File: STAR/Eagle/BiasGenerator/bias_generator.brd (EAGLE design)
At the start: 54.6 x 29.8 mm, 24 parts, among them J1 J30J-9J30, T1 750311838, U1 LT8300, U2 LT8330

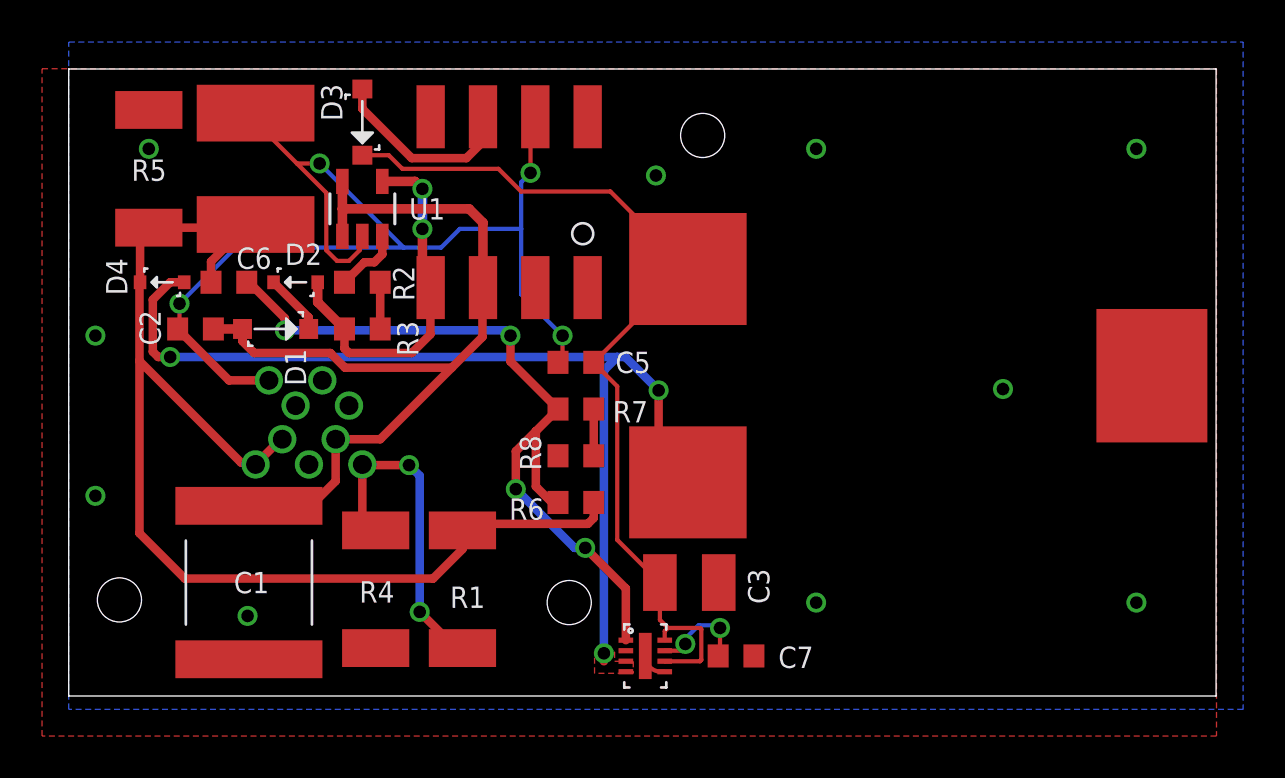
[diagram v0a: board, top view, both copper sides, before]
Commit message: Finished routing new bias board rev 2.0. Fixed the choke configuration on that board.
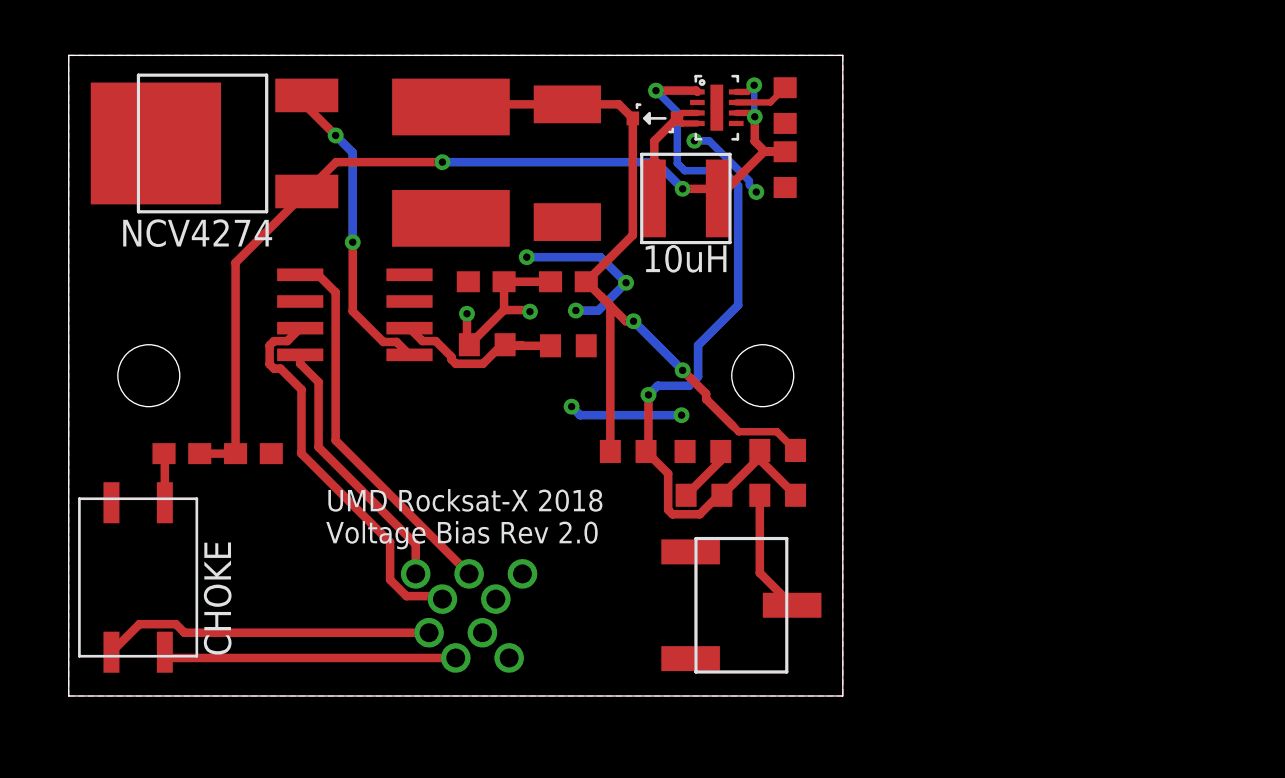
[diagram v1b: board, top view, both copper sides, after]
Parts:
- removed C1: 22uF, AR_passives:3025
- removed C2, C5, C7: 1uF, AR_passives:0603
- removed C3: (no value), resistor:C1210
- removed C4: 10uF, AR_passives:2J-LEAD
- removed C6: 4.7pF, AR_passives:0603
- removed D1: MMSZ5266BT1G, AR_diode:SOD123
- removed D2: BAV20W, AR_diode:SOD323
- removed D3: SBR0560S1, AR_diode:SOD123
- removed D4: PMEG6010CEJ, AR_diode:SOD323
- removed L1: 10uH, AR_passives:PQ2614
- removed R1: 47k, resistor:R2512
- removed R2: 407k, resistor:R0603
- removed R3: 1k, resistor:R0603
- removed R4: 3k, resistor:R2512
- removed R5: 1.5k, resistor:R2512
- removed R6: 1M, resistor:R0603
- removed R7: 33k, resistor:R0603
- removed R8: 52.6, resistor:R0603
- removed T1: 750311838, AR_transformer:750311838
- removed U1: LT8300, AR_IC:SOT23-5
- removed U2: LT8330, AR_IC:8-DFN
- added CHOKE: DFT7160-105B, Filtering:DFT7160
- added C_GND, C_VCC: .1uF, resistor:C0603
- added C_LAD: 4.7pF, AR_passives:0603
- added C_LTIN, C_LTREQ: 1uF, AR_passives:0603
- added C_LTOUT: 10uF, AR_passives:2J-LEAD
- added D_LT: PMEG6010CEJ, AR_diode:SOD323
- added ISO: AMC1311-Q1, Filtering:SOIC8
- added L_LT: ASPI-4020S-100M-T, AR_passives:4MM
- added L_VCC, L_VOUT: 82nH, resistor:C0603
- added REG: NCV4274ADT50RKG, Filtering:DPAK
- added R_DIV1: 500k, resistor:R0603
- added R_DIV2: 25k, resistor:R0603
- added R_LAD1: 1M, resistor:R0603
- added R_LAD2: 33k, resistor:R0603
- added R_LAD3: 52.6, resistor:R0603
- added R_LTOUT: 1.5k, resistor:R2512
- added R_POT1: 20k, resistor:R0603
- added R_POT2: 3269W-1-503LF, Filtering:POTENTIOMETER
- added SWITCH: LT8330, AR_IC:8-DFN
- moved J1 12.0 mm to (19.1, 3.81), turned to 180 degrees
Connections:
- removed net +20V: C3.1, C5.1, D3.P$2, L1.P$2, U2.P$6, U2.P$8
- removed net N$10: J1.9
- removed net N$3: R2.2, R3.1
- removed net N$4: D2.P$1, R3.2, T1.P$4, U1.4
- removed net N$5: D3.P$1, T1.P$6
- removed net N$6: C7.1, U2.P$7
- removed net N$7: D4.P$1, L1.P$3, U2.P$3, U2.P$4
- removed net N$9: C6.2, R6.1, R7.2, U2.P$1
- new net +50V_FILT: C_GND.1, J1.1, J1.2, L_VOUT.2, R_DIV1.2
- new net 5V_REG: ISO.1, REG.P$3
- new net FBX: C_LAD.2, R_LAD1.1, R_LAD2.2, R_POT1.2, SWITCH.P$1
- new net GND_IN: CHOKE.P$1, J1.9
- new net INTVCC: C_LTREQ.1, SWITCH.P$7
- new net STAR_3V3: ISO.8, J1.5
- new net STAR_GND: ISO.5, J1.3
- new net SW: D_LT.P$1, L_LT.P$2, SWITCH.P$3, SWITCH.P$4
- new net VCC_FILT: C_LTIN.1, C_VCC.1, L_LT.P$1, L_VCC.2, REG.P$1, SWITCH.P$6, SWITCH.P$8
- new net V_SENSE: ISO.7, J1.4
- net +50V: now also C_LAD.1, C_LTOUT.P$1, D_LT.P$2, L_VOUT.1, R_LAD1.2, R_LTOUT.2; no longer C4.P$1, C6.1, D4.P$2, J1.1, J1.2, R1.2, R5.2, R6.2
- net GND: now also CHOKE.P$4, C_GND.2, C_LTIN.2, C_LTOUT.P$2, C_LTREQ.2, C_VCC.2, ISO.4, REG.P$4, R_DIV2.1, R_LAD3.1, R_LTOUT.1, R_POT2.P$3, SWITCH.P$5, SWITCH.P$9; no longer C1.P$2, C2.2, C3.2, C4.P$2, C5.2, C7.2, R4.1, R5.1, R8.1, T1.P$7, U1.2, U2.P$5, U2.P$9
- net N$1: now also CHOKE.P$3, L_VCC.1; no longer D1.P$2, D2.P$2
- net N$11: now also R_LAD2.1, R_LAD3.2; no longer R7.1, R8.2
- net N$2: now also R_POT1.1, R_POT2.P$2; no longer R2.1, U1.3
- net VCC: now also CHOKE.P$2, J1.8; no longer C1.P$1, C2.1, D1.P$1, J1.4, T1.P$3, U1.1, U1.5
- net V_DIVIDE: now also ISO.2, R_DIV1.1, R_DIV2.2; no longer J1.5, R1.1, R4.2
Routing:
- net N$7: track 48.8 -> 0.00 mm, vias 3 -> 0
- net VCC_FILT: track 0.00 -> 46.8 mm, vias 0 -> 4
- net +20V: track 43.6 -> 0.00 mm
- net GND: track 55.8 -> 17.6 mm, vias 14 -> 7
- net N$9: track 36.7 -> 0.00 mm, vias 4 -> 0
- net FBX: track 0.00 -> 36.5 mm, vias 0 -> 2
- net VCC: track 43.1 -> 14.0 mm
- net +50V: track 57.6 -> 38.7 mm, vias 0 -> 2
- net V_SENSE: track 0.00 -> 18.4 mm
- net STAR_GND: track 0.00 -> 18.1 mm
- net N$4: track 17.4 -> 0.00 mm, vias 2 -> 0
- net GND_IN: track 0.00 -> 15.8 mm
- net 5V_REG: track 0.00 -> 14.7 mm, vias 0 -> 2
- net STAR_3V3: track 0.00 -> 12.7 mm
- net N$5: track 9.16 -> 0.00 mm
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- added copper zone on layer 16, net +50V_FILT
- removed copper zone on layer 16, net GND
- removed copper zone on layer 1, net N$7
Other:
- board size 54.6 x 29.8 mm -> 36.8 x 30.5 mm
- board text added: "10uH"
- board text added: "NCV4274"
- board text added: "UMD Rocksat-X 2018 Voltage Bias Rev 2.0"
- board text removed: "Bias Generator"
- board text removed: "Jan. 2017"
- board text removed: "Rev. 1"

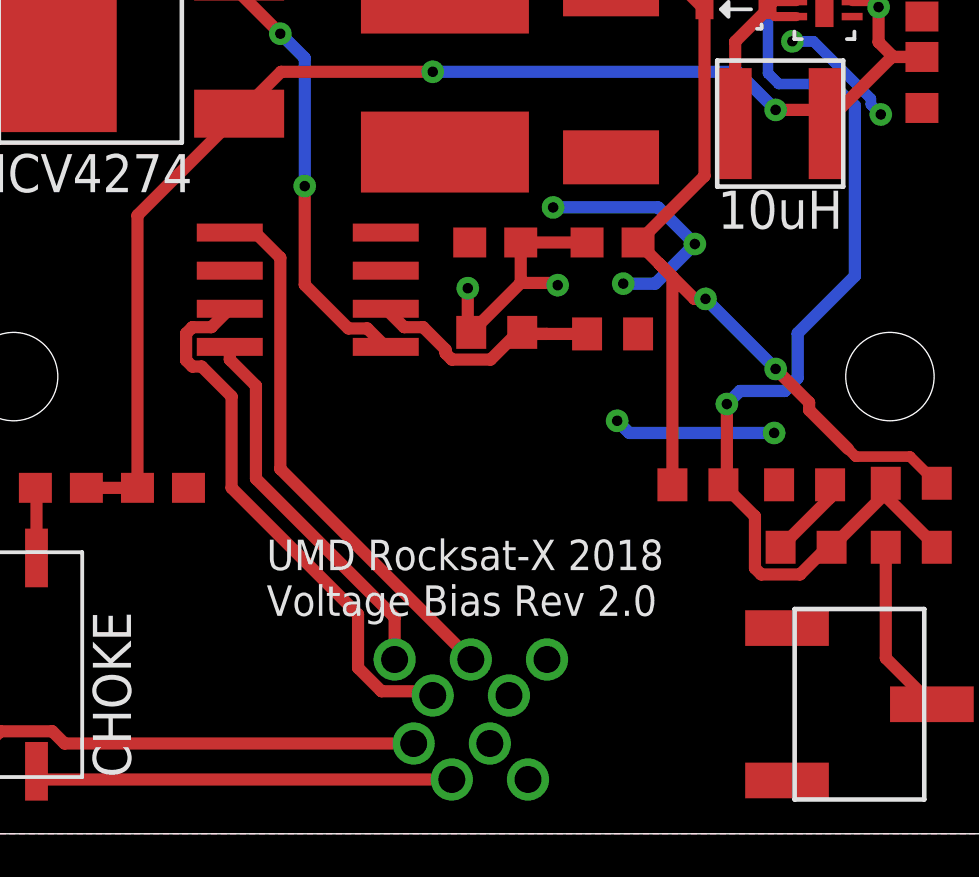
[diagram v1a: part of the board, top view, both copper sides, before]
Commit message: Updated bias board and libraries to reflect the actual package used by the analog isolator
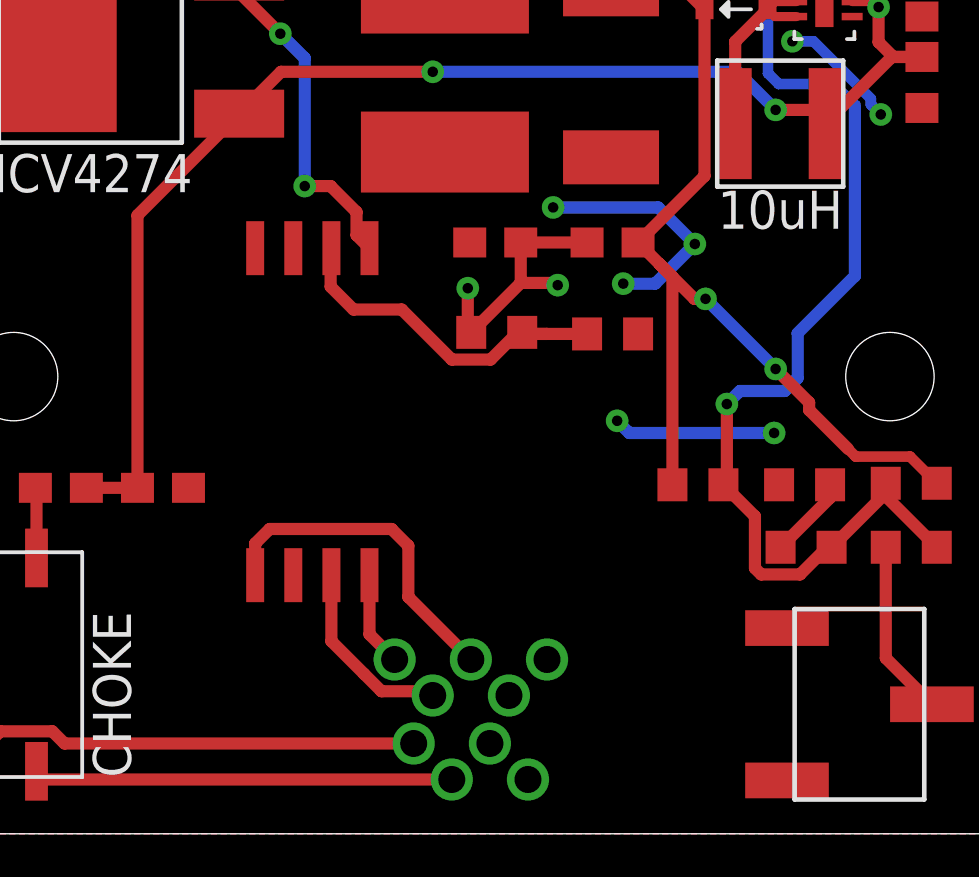
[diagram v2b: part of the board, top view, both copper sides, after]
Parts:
- R_DIV1: value 500k -> 402k
- R_DIV2: value 25k -> 12k
- moved ISO 4.07 mm to (13.8, 14.1), turned to 180 degrees
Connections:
- net GND: now also ISO.3
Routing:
- net V_SENSE: track 18.4 -> 6.33 mm
- net STAR_3V3: track 12.7 -> 3.16 mm
- net STAR_GND: track 18.1 -> 11.2 mm
- net 5V_REG: track 14.7 -> 11.4 mm
- net V_DIVIDE: track 8.69 -> 12.1 mm
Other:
- board text added: "UMD Rocksat-X 2018 Voltage Bias Rev 2.1"
- board text removed: "UMD Rocksat-X 2018 Voltage Bias Rev 2.0"
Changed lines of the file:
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@@
 <hole x="3.81" y="15.24" drill="2.9464"/>
 <hole x="33.02" y="15.24" drill="2.9464"/>
-<text x="12.2428" y="7.2644" size="1.016" layer="21" font="vector">UMD Rocksat-X 2018
-Voltage Bias Rev 2.0</text>
+<text x="25.8064" y="7.112" size="1.016" layer="22" font="vector" rot="MR0">UMD Rocksat-X 2018
+Voltage Bias Rev 2.1</text>
 <text x="27.2796" y="20.1676" size="1.27" layer="21">10uH</text>
 <text x="2.4384" y="21.3868" size="1.27" layer="21">NCV4274</text>
@@
 </element>
 <element name="R_POT2" library="Filtering" package="POTENTIOMETER" value="3269W-1-503LF" x="28.194" y="4.318" rot="R270"/>
-<element name="ISO" library="Filtering" package="SOIC8" value="AMC1311-Q1" x="13.6144" y="18.1356" smashed="yes" rot="R90">
-<attribute name="VALUE" x="11.4554" y="18.7706" size="1.27" layer="27" rot="R180"/>
+<element name="ISO" library="Filtering" package="SOIC8" value="AMC1311-Q1" x="13.7668" y="14.0716" smashed="yes" rot="R180">
+<attribute name="VALUE" x="16.2306" y="19.2786" size="1.27" layer="27" rot="R270"/>
 </element>
 <element name="L_LT" library="AR_passives" package="4MM" value="ASPI-4020S-100M-T" x="29.3624" y="23.6728" rot="R180"/>
 <element name="SWITCH" library="AR_IC" package="8-DFN" value="LT8330" x="30.8356" y="27.9908" rot="R270"/>
 <element name="REG" library="Filtering" package="DPAK" value="NCV4274ADT50RKG" x="12.827" y="26.289"/>
-<element name="R_DIV1" library="resistor" package="R0603" value="500k" x="19.9136" y="16.7132" smashed="yes" rot="R180">
+<element name="R_DIV1" library="resistor" package="R0603" value="402k" x="19.9136" y="16.7132" smashed="yes" rot="R180">
 <attribute name="VALUE" x="21.5646" y="15.4686" size="1.27" layer="27" rot="R180"/>
 </element>
-<element name="R_DIV2" library="resistor" package="R0603" value="25k" x="23.7744" y="16.6624" smashed="yes" rot="R180">
+<element name="R_DIV2" library="resistor" package="R0603" value="12k" x="23.7744" y="16.6624" smashed="yes" rot="R180">
 <attribute name="VALUE" x="24.8666" y="15.4686" size="1.27" layer="27" rot="R180"/>
 </element>
@@
 <wire x1="32.385" y1="24.50334375" x2="30.47234375" y2="26.416" width="0.3556" layer="16"/>
 <wire x1="30.47234375" y1="26.416" x2="29.7688" y2="26.416" width="0.3556" layer="16"/>
+<contactref element="ISO" pad="3"/>
 </signal>
 <signal name="VCC_FILT">
@@
 <wire x1="20.8144" y1="16.6624" x2="21.59" y2="16.6624" width="0.4064" layer="1"/>
 <wire x1="21.59" y1="16.6624" x2="22.9244" y2="16.6624" width="0.4064" layer="1"/>
-<wire x1="16.2144" y1="17.5006" x2="16.8288" y2="16.8862" width="0.4064" layer="1"/>
-<wire x1="16.8288" y1="16.8862" x2="17.46169375" y2="16.8862" width="0.4064" layer="1"/>
-<wire x1="18.208" y1="16.01590625" x2="18.41630625" y2="15.8076" width="0.4064" layer="1"/>
 <wire x1="18.41630625" y1="15.8076" x2="19.71089375" y2="15.8076" width="0.4064" layer="1"/>
-<wire x1="18.208" y1="16.13989375" x2="18.208" y2="16.01590625" width="0.4064" layer="1"/>
 <wire x1="20.56569375" y1="16.6624" x2="21.59" y2="16.6624" width="0.4064" layer="1"/>
-<wire x1="17.46169375" y1="16.8862" x2="18.208" y2="16.13989375" width="0.4064" layer="1"/>
 <wire x1="19.71089375" y1="15.8076" x2="20.56569375" y2="16.6624" width="0.4064" layer="1"/>
+<wire x1="18.41630625" y1="15.8076" x2="16.74870625" y2="17.4752" width="0.4064" layer="1"/>
+<wire x1="16.74870625" y1="17.4752" x2="15.1384" y2="17.4752" width="0.4064" layer="1"/>
+<wire x1="15.1384" y1="17.4752" x2="14.3764" y2="18.2372" width="0.4064" layer="1"/>
+<wire x1="14.3764" y1="18.2372" x2="14.3764" y2="19.4962" width="0.4064" layer="1"/>
+<wire x1="14.3764" y1="19.4962" x2="14.4018" y2="19.5216" width="0.4064" layer="1"/>
 </signal>
 <signal name="STAR_3V3">
 <contactref element="ISO" pad="8"/>
 <contactref element="J1" pad="5"/>
-<wire x1="16.51" y1="5.81" x2="16.51" y2="7.2136" width="0.4064" layer="1"/>
-<wire x1="11.8872" y1="11.8364" x2="11.8872" y2="14.9352" width="0.4064" layer="1"/>
-<wire x1="11.8872" y1="14.9352" x2="11.0144" y2="15.808" width="0.4064" layer="1"/>
-<wire x1="11.0144" y1="15.808" x2="11.0144" y2="16.2306" width="0.4064" layer="1"/>
-<wire x1="16.51" y1="7.2136" x2="11.8872" y2="11.8364" width="0.4064" layer="1"/>
+<wire x1="15.6718" y1="8.6216" x2="15.6718" y2="6.6482" width="0.4064" layer="1"/>
+<wire x1="15.6718" y1="6.6482" x2="16.51" y2="5.81" width="0.4064" layer="1"/>
 </signal>
 <signal name="N$1">
@@
 <contactref element="REG" pad="P$3"/>
 <via x="13.5128" y="21.59" extent="1-16" drill="0.35"/>
-<wire x1="16.2144" y1="16.2306" x2="15.6" y2="16.845" width="0.4064" layer="1"/>
-<wire x1="15.6" y1="16.845" x2="14.96710625" y2="16.845" width="0.4064" layer="1"/>
-<wire x1="14.96710625" y1="16.845" x2="13.5128" y2="18.29930625" width="0.4064" layer="1"/>
-<wire x1="13.5128" y1="18.29930625" x2="13.5128" y2="21.59" width="0.4064" layer="1"/>
 <wire x1="13.5128" y1="21.59" x2="13.5128" y2="25.8572" width="0.4064" layer="16"/>
 <wire x1="13.5128" y1="25.8572" x2="12.7" y2="26.67" width="0.4064" layer="16"/>
@@
 <wire x1="12.7" y1="26.67" x2="11.327" y2="28.043" width="0.4064" layer="1"/>
 <wire x1="11.327" y1="28.043" x2="11.327" y2="28.574" width="0.4064" layer="1"/>
+<wire x1="15.6718" y1="19.5216" x2="15.24" y2="19.9534" width="0.4064" layer="1"/>
+<wire x1="15.24" y1="19.9534" x2="15.24" y2="20.7264" width="0.4064" layer="1"/>
+<wire x1="15.24" y1="20.7264" x2="14.3764" y2="21.59" width="0.4064" layer="1"/>
+<wire x1="14.3764" y1="21.59" x2="13.5128" y2="21.59" width="0.4064" layer="1"/>
 </signal>
 <signal name="V_SENSE">
@@
 <wire x1="17.78" y1="4.61" x2="17.6396" y2="4.7504" width="0.4064" layer="1"/>
 <wire x1="17.6396" y1="4.7504" x2="16.07109375" y2="4.7504" width="0.4064" layer="1"/>
-<wire x1="16.07109375" y1="4.7504" x2="15.2908" y2="5.53069375" width="0.4064" layer="1"/>
-<wire x1="15.2908" y1="5.53069375" x2="15.2908" y2="7.3152" width="0.4064" layer="1"/>
-<wire x1="15.2908" y1="7.3152" x2="11.0744" y2="11.5316" width="0.4064" layer="1"/>
-<wire x1="11.0744" y1="11.5316" x2="11.0744" y2="14.5796" width="0.4064" layer="1"/>
-<wire x1="9.76710625" y1="15.575" x2="9.5588" y2="15.78330625" width="0.4064" layer="1"/>
-<wire x1="9.5588" y1="15.78330625" x2="9.5588" y2="16.67789375" width="0.4064" layer="1"/>
-<wire x1="9.5588" y1="16.67789375" x2="9.76710625" y2="16.8862" width="0.4064" layer="1"/>
-<wire x1="9.76710625" y1="16.8862" x2="10.4" y2="16.8862" width="0.4064" layer="1"/>
-<wire x1="10.4" y1="16.8862" x2="11.0144" y2="17.5006" width="0.4064" layer="1"/>
-<wire x1="10.079" y1="15.575" x2="9.76710625" y2="15.575" width="0.4064" layer="1"/>
-<wire x1="11.0744" y1="14.5796" x2="10.079" y2="15.575" width="0.4064" layer="1"/>
+<wire x1="16.07109375" y1="4.7504" x2="15.490746875" y2="5.330746875" width="0.4064" layer="1"/>
+<wire x1="15.490746875" y1="5.330746875" x2="14.4018" y2="6.41969375" width="0.4064" layer="1"/>
+<wire x1="14.4018" y1="6.41969375" x2="14.4018" y2="8.6216" width="0.4064" layer="1"/>
 </signal>
 <signal name="STAR_GND">
 <contactref element="ISO" pad="5"/>
 <contactref element="J1" pad="3"/>
-<wire x1="19.05" y1="5.81" x2="12.7" y2="12.16" width="0.4064" layer="1"/>
-<wire x1="12.7" y1="12.16" x2="12.7" y2="19.2024" width="0.4064" layer="1"/>
-<wire x1="12.7" y1="19.2024" x2="11.8618" y2="20.0406" width="0.4064" layer="1"/>
-<wire x1="11.8618" y1="20.0406" x2="11.0144" y2="20.0406" width="0.4064" layer="1"/>
+<wire x1="19.05" y1="5.81" x2="16.9672" y2="7.8928" width="0.4064" layer="1"/>
+<wire x1="16.9672" y1="7.8928" x2="16.9672" y2="9.6012" width="0.4064" layer="1"/>
+<wire x1="16.9672" y1="9.6012" x2="16.4084" y2="10.16" width="0.4064" layer="1"/>
+<wire x1="11.8618" y1="9.6774" x2="11.8618" y2="8.6216" width="0.4064" layer="1"/>
+<wire x1="16.4084" y1="10.16" x2="12.3444" y2="10.16" width="0.4064" layer="1"/>
+<wire x1="12.3444" y1="10.16" x2="11.8618" y2="9.6774" width="0.4064" layer="1"/>
 </signal>
 <signal name="GND_IN">
